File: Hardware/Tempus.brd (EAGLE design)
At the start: 37 x 50 mm, 36 parts, among them J7 AVR_SPI_PRG_6NS, U1 ATMEGA328P_TQFP, Y1 16MHZ

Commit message: Hardware modifications
Hardware modifications
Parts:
- removed J1, J10, J11, J12, J13, J14, J15, J17, J18, J19, J2, J20, J21, J22, J23, J24, J25, J3, J4, J5, J6, J8, J9: (no value), SparkFun-Connectors:1X01NS-KIT
- removed J16: (no value), SparkFun-Connectors:1X06_NO_SILK
- added U$1: DISP_TFT18, KarlVaello-Displays:TFT18
- moved Y1 28.8 mm to (24.3, 29.9), flipped to the bottom
- moved C1 28.7 mm to (25.1, 33.2), flipped to the bottom, turned to 0 degrees
- moved C3 28.1 mm to (26.3, 36.8), flipped to the bottom, turned to 0 degrees
- moved LED1 23.7 mm to (8.10, 25.7), flipped to the bottom, turned to 0 degrees
- moved S1 23.4 mm to (26.5, 41.2), flipped to the bottom, turned to 0 degrees
- moved C2 22.4 mm to (8.90, 31.8), flipped to the bottom
- moved U1 22.3 mm to (17.0, 32.3), flipped to the bottom
- moved R4 22.2 mm to (17.5, 40.4), flipped to the bottom
- moved R3 21.4 mm to (12.2, 41.3), flipped to the bottom, turned to 0 degrees
- moved R2 18.8 mm to (12.1, 38.6), flipped to the bottom, turned to 0 degrees
- moved R1 17.8 mm to (11.5, 25.5), flipped to the bottom, turned to 90 degrees
- moved J7 17.4 mm to (15.1, 19.5), turned to 180 degrees
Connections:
- net A0: no longer J1.1
- net A1: no longer J2.1
- net A2: no longer J3.1
- net A3: no longer J17.1
- net A4: no longer J20.1
- net A5: no longer J21.1
- net A6: no longer J18.1
- net A7: no longer J19.1
- net D10: no longer J6.1
- net D2: no longer J11.1
- net D3: no longer J12.1
- net D4: no longer J13.1
- net D5: no longer J14.1
- net D6: no longer J15.1
- net D7: no longer J8.1
- net D8: no longer J4.1
- net D9: no longer J5.1
- net DTR: no longer J16.1
- net GND: no longer J16.5, J16.6, J24.1, J25.1
- net RXI: no longer J16.3, J9.1
- net TXO: no longer J10.1, J16.2
- net VCC: no longer J16.4, J22.1, J23.1
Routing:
- net VCC: track 52.8 -> 0.00 mm, vias 2 -> 0
- net RESET: track 33.5 -> 0.00 mm, vias 2 -> 0
- net RXI: track 23.7 -> 0.00 mm, vias 1 -> 0
- net TXO: track 22.1 -> 0.00 mm, vias 3 -> 0
- net A7: track 20.0 -> 0.00 mm, vias 1 -> 0
- net D4: track 19.9 -> 0.00 mm, vias 1 -> 0
- net A6: track 19.5 -> 0.00 mm, vias 1 -> 0
- net D3: track 17.8 -> 0.00 mm, vias 1 -> 0
- net A0: track 15.9 -> 0.00 mm
- net A1: track 13.5 -> 0.00 mm, vias 1 -> 0
- net A5: track 13.4 -> 0.00 mm, vias 1 -> 0
- net SCK: track 12.8 -> 0.00 mm, vias 1 -> 0
- net D2: track 12.6 -> 0.00 mm, vias 1 -> 0
- net DTR: track 12.1 -> 0.00 mm, vias 2 -> 0
- net MOSI: track 12.1 -> 0.00 mm, vias 1 -> 0
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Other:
- board size 37 x 50 mm -> 34 x 46 mm

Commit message: Hardware modifications
Hardware modifications
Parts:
- removed J7: AVR_SPI_PRG_6NS, SparkFun-Connectors:2X3-NS
- added J1: AVR_SPI_PRG_6TESTPOINTS, SparkFun-Connectors:2X3_TEST_POINTS
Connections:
- net GND: now also J1.6; no longer J7.6
- net MISO: now also J1.1; no longer J7.1
- net MOSI: now also J1.4; no longer J7.4
- net RST: now also J1.5; no longer J7.5
- net SCK: now also J1.3; no longer J7.3
- net VCC: now also J1.2; no longer J7.2
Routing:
- net GND: track 2.67 -> 0.00 mm
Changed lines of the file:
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@@
 <attribute name="PROD_ID" value="SWCH-08247" x="26.5" y="41.2" size="1.778" layer="28" rot="MR0" display="off"/>
 </element>
-<element name="J7" library="SparkFun-Connectors" package="2X3-NS" value="AVR_SPI_PRG_6NS" x="15.08" y="19.54" rot="R180"/>
 <element name="LED1" library="adafruit" package="CHIPLED_0805" value="" x="8.1" y="25.7" rot="MR0"/>
 <element name="Y1" library="SparkFun-FreqCtrl" package="RESONATOR-SMD" value="16MHZ" x="24.3" y="29.9" rot="MR270">
@@
 </element>
 <element name="U$1" library="KarlVaello-Displays" package="TFT18" value="DISP_TFT18" x="17" y="24.5" rot="R270"/>
+<element name="J1" library="SparkFun-Connectors" package="2X3_TEST_POINTS" value="AVR_SPI_PRG_6TESTPOINTS" x="8.5" y="19.6"/>
 </elements>
 <signals>
@@
 <contactref element="S1" pad="2"/>
 <contactref element="S1" pad="1"/>
-<contactref element="J7" pad="6"/>
 <contactref element="LED1" pad="C"/>
 <contactref element="Y1" pad="2"/>
-<wire x1="23.37" y1="3" x2="20.7" y2="3" width="0.25" layer="1"/>
+<contactref element="J1" pad="6"/>
 </signal>
 <signal name="RESET">
@@
 <contactref element="R2" pad="2"/>
 <contactref element="R3" pad="2"/>
-<contactref element="J7" pad="2"/>
+<contactref element="J1" pad="2"/>
 <wire x1="11.25" y1="41.3" x2="17.5" y2="41.35" width="0" layer="19" extent="16-16"/>
 <wire x1="11.15" y1="38.6" x2="11.25" y2="41.3" width="0" layer="19" extent="16-16"/>
@@
 <wire x1="21.2926" y1="32.7" x2="21.2926" y2="31.1" width="0" layer="19" extent="16-16"/>
 <wire x1="24.15" y1="33.2" x2="21.2926" y2="32.7" width="0" layer="19" extent="16-16"/>
-<wire x1="17.62" y1="18.27" x2="12.7074" y2="30.3" width="0" layer="19" extent="16-16"/>
+<wire x1="5.96" y1="20.87" x2="12.7074" y2="30.3" width="0" layer="19" extent="16-16"/>
 </signal>
 <signal name="A4">
@@
 <contactref element="U1" pad="17"/>
 <contactref element="R1" pad="2"/>
-<contactref element="J7" pad="3"/>
+<contactref element="J1" pad="3"/>
 <wire x1="11.5" y1="26.45" x2="12.7074" y2="29.5" width="0" layer="19" extent="16-16"/>
-<wire x1="15.08" y1="20.81" x2="11.5" y2="26.45" width="0" layer="19" extent="16-16"/>
+<wire x1="8.5" y1="18.33" x2="11.5" y2="26.45" width="0" layer="19" extent="16-16"/>
 </signal>
 <signal name="A0">
@@
 <signal name="MOSI">
 <contactref element="U1" pad="15"/>
-<contactref element="J7" pad="4"/>
-<wire x1="15.08" y1="18.27" x2="15" y2="28.0074" width="0" layer="19" extent="16-16"/>
+<contactref element="J1" pad="4"/>
+<wire x1="8.5" y1="20.87" x2="15" y2="28.0074" width="0" layer="19" extent="16-16"/>
 </signal>
 <signal name="MISO">
 <contactref element="U1" pad="16"/>
-<contactref element="J7" pad="1"/>
-<wire x1="17.62" y1="20.81" x2="14.2" y2="28.0074" width="0" layer="19" extent="16-16"/>
+<contactref element="J1" pad="1"/>
+<wire x1="5.96" y1="18.33" x2="14.2" y2="28.0074" width="0" layer="19" extent="16-16"/>
 </signal>
 <signal name="D9">
 <contactref element="U1" pad="13"/>
-</signal>
-<signal name="RST">
-<contactref element="J7" pad="5"/>
 </signal>
 <signal name="N$1">
@@
 <wire x1="23" y1="31.1" x2="24.3" y2="31.1" width="0.3" layer="16"/>
 </signal>
+<signal name="RST">
+<contactref element="J1" pad="5"/>
+</signal>
 </signals>

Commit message: Hardware
Hardware
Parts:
- removed LED1: (no value), adafruit:CHIPLED_0805
- removed R1, R2, R3: (no value), KarlVaello-Resistors:R0805
- added C4: (no value), KarlVaello-Capacitors:C1608
- added C5, C8: (no value), KarlVaello-Capacitors:A/3216-18R
- added J2: (no value), SparkFun-Connectors:1X06
- added R5, R6, R7: (no value), KarlVaello-Resistors:R0603
- added U$2, U$3, U$4: MICRO_SIDE_TACT_BUTTON_SMD_SECURE, KarlVaello-ElectroMechanical:MICRO_SIDE_TACT_BUTTON_SMD_SECURE
- added U$5: (no value), bc417:BTM400_6B
- added U2: MIC5205, SparkFun-PowerIC:SOT23-5
- C1, C2, C3: device KarlVaello-Capacitors:C0805 -> KarlVaello-Capacitors:C1608
- R4: device KarlVaello-Resistors:R0805 -> KarlVaello-Resistors:R0603
- moved S1 35.9 mm to (23.0, 5.50), turned to 180 degrees
- moved C3 25.2 mm to (26.7, 11.6), turned to 180 degrees
- moved R4 19.3 mm to (27.1, 23.6), turned to 180 degrees
- moved J1 14.1 mm to (5.60, 5.80), turned to 270 degrees
- moved Y1 13.2 mm to (24.5, 16.7)
- moved U1 13.2 mm to (17.0, 19.1)
- moved C1 12.1 mm to (27.1, 21.3), turned to 180 degrees
- moved C2 11.5 mm to (8.00, 20.3)
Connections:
- net RXI renamed D0/RXI
- net TXO renamed D1/TXO
- removed net D10: U1.14
- removed net MISO: J1.1, U1.16
- removed net MOSI: J1.4, U1.15
- removed net N$1: LED1.A, R1.1
- removed net RST: J1.5
- removed net SCK: J1.3, R1.2, U1.17
- new net 3.3V: U$5.3.3V
- new net D10/SS: U$1.8, U1.14
- new net D11/MOSI: J1.4, U$1.9, U1.15
- new net D12/MISO: J1.1, U$1.12, U1.16
- new net D13/SCK: J1.3, U1.17
- new net LIPO: C5.+, U2.1, U2.3
- new net N$11: U$1.1
- new net N$12: U$1.14
- net A4: no longer R2.1
- net A5: no longer R3.1
- net D2: now also U$5.UART-TX
- net D3: now also U$5.UART-RX
- net D4: now also R5.2, U$4.P$1
- net D5: now also R6.2, U$2.P$1
- net D6: now also R7.2, U$3.P$1
- net D8: now also U$1.6
- net D9: now also U$1.7
- net GND: now also C4.1, C5.-, C8.-, R5.1, R6.1, R7.1, U$1.13, U$1.2, U$1.4, U$1.5, U$5.GND@1, U$5.GND@2, U$5.GND@3, U$5.GND@4, U2.2; no longer LED1.C
- net RESET: now also J1.5
- net VCC: now also C4.2, C8.+, U$1.10, U$1.11, U$1.3, U$2.P$2, U$3.P$2, U$4.P$2, U2.5; no longer R2.2, R3.2
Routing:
- net VCC: track 0.00 -> 111.7 mm, vias 0 -> 3
- net RESET: track 0.00 -> 65.1 mm, vias 0 -> 3
- net D6: track 0.00 -> 53.8 mm, vias 0 -> 2
- net D3: track 0.00 -> 35.3 mm, vias 0 -> 2
- net D2: track 0.00 -> 33.2 mm, vias 0 -> 2
- net D11/MOSI: track 0.00 -> 30.1 mm
- net D4: track 0.00 -> 29.2 mm, vias 0 -> 2
- net D12/MISO: track 0.00 -> 28.3 mm
- net D5: track 0.00 -> 18.0 mm
- net D13/SCK: track 0.00 -> 17.8 mm
- net D10/SS: track 0.00 -> 10.9 mm, vias 0 -> 1
- net D8: track 0.00 -> 10.0 mm, vias 0 -> 1
- net D9: track 0.00 -> 7.54 mm, vias 0 -> 1
- net LIPO: track 0.00 -> 7.16 mm
- net N$3: track 0.00 -> 4.75 mm

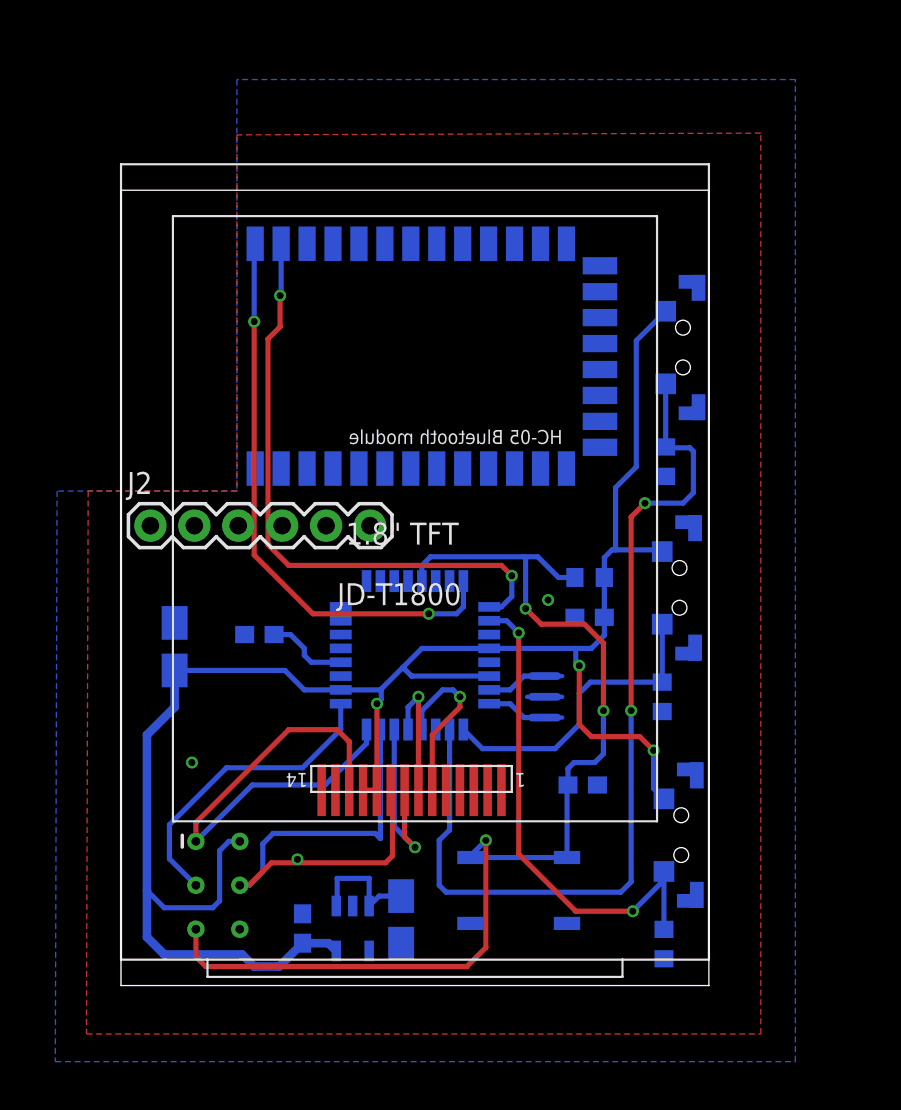
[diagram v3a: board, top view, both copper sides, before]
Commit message: Hardware modifications
Hardware modifications. Tempus now based on ARM 32-bit, 3.3V at 48Mhz
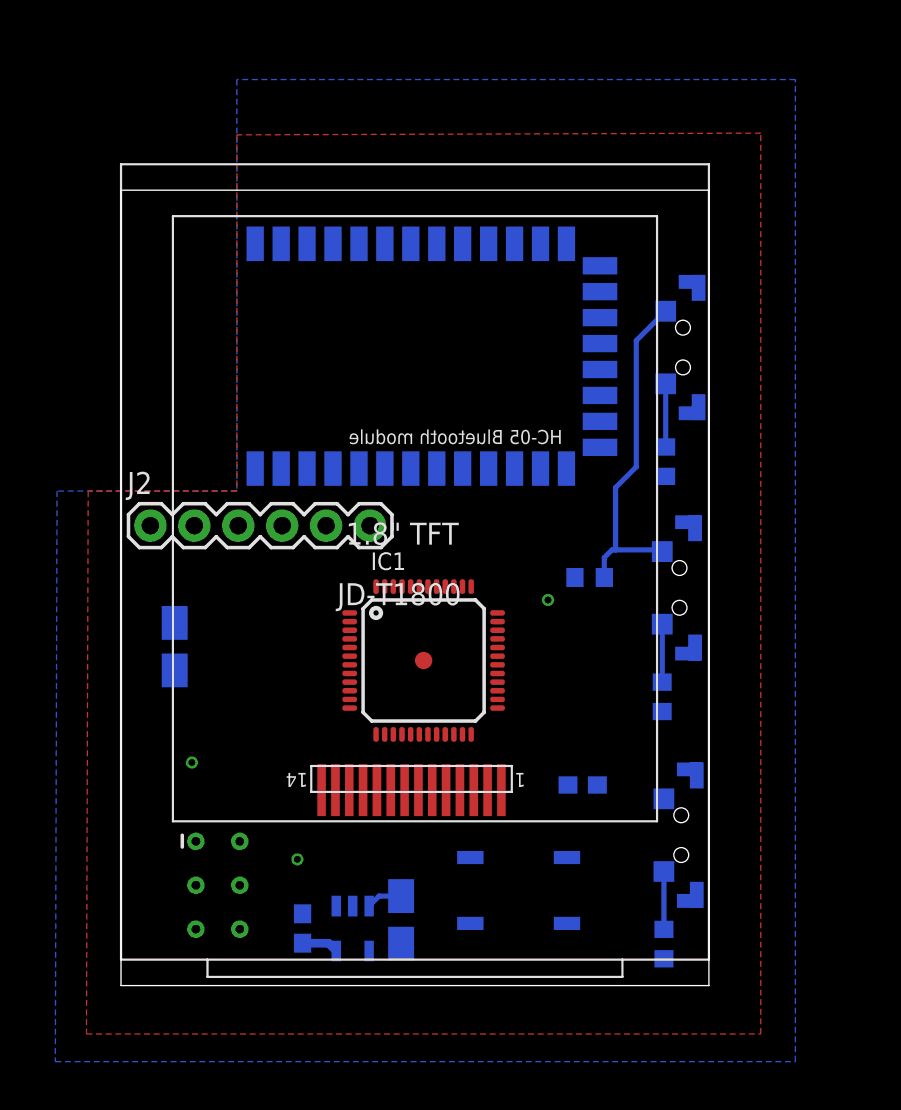
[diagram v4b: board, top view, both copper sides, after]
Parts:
- removed C1, C2: (no value), KarlVaello-Capacitors:C1608
- removed U1: ATMEGA328P_TQFP, KarlVaello-DigitalIC:TQFP32-08
- removed Y1: 16MHZ, SparkFun-FreqCtrl:RESONATOR-SMD
- added IC1: SAMD21G18A-AUT, KarlVaello-DigitalIC:TQFP48-7X7
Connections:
- removed net A0: U1.23
- removed net A1: U1.24
- removed net A2: U1.25
- removed net A3: U1.26
- removed net A4: U1.27
- removed net A5: U1.28
- removed net A6: U1.19
- removed net A7: U1.22
- removed net D0/RXI: U1.30
- removed net D1/TXO: U1.31
- removed net D7: U1.11
- removed net N$2: U1.8, Y1.3
- removed net N$3: C2.2, U1.20
- removed net N$6: U1.7, Y1.1
- new net GND1: IC1.18
- new net GND2: IC1.35
- new net GND3: IC1.42
- new net GNDANA: IC1.5
- new net VDDANA: IC1.6
- new net VDDIN: IC1.44
- new net VDDIO1: IC1.17
- new net VDDIO2: IC1.36
- net D10/SS: no longer U1.14
- net D11/MOSI: no longer U1.15
- net D12/MISO: no longer U1.16
- net D13/SCK: no longer U1.17
- net D2: no longer U1.32
- net D3: no longer U1.1
- net D4: no longer U1.2
- net D5: no longer U1.9
- net D6: no longer U1.10
- net D8: no longer U1.12
- net D9: no longer U1.13
- net GND: no longer C1.1, C2.1, U1.21, U1.3, U1.5, Y1.2
- net RESET: no longer U1.29
- net VCC: no longer C1.2, U1.18, U1.4, U1.6
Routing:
- net VCC: track 111.7 -> 21.9 mm, vias 3 -> 0
- net RESET: track 65.1 -> 0.00 mm, vias 3 -> 0
- net D6: track 53.8 -> 3.65 mm, vias 2 -> 0
- net D3: track 35.3 -> 0.00 mm, vias 2 -> 0
- net D2: track 33.2 -> 0.00 mm, vias 2 -> 0
- net D11/MOSI: track 30.1 -> 0.00 mm
- net D12/MISO: track 28.3 -> 0.00 mm
- net D4: track 29.2 -> 3.35 mm, vias 2 -> 0
- net D13/SCK: track 17.8 -> 0.00 mm
- net D5: track 18.0 -> 3.35 mm
- net D10/SS: track 10.9 -> 0.00 mm, vias 1 -> 0
- net D8: track 10.0 -> 0.00 mm, vias 1 -> 0
- net D9: track 7.54 -> 0.00 mm, vias 1 -> 0
- net LIPO: track 7.16 -> 2.09 mm
- net N$3: track 4.75 -> 0.00 mm
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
